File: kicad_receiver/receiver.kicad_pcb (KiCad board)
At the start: 2 copper layers, 60 x 50 mm, 64 parts, among them J1 Conn_01x05_Male, J2 M1+, J3 M1-, J4 M2+, J5 M2-, J6 CHG+5V, J7 CHG-, J8 BAT+, J9 BAT-, Q1 BSS138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

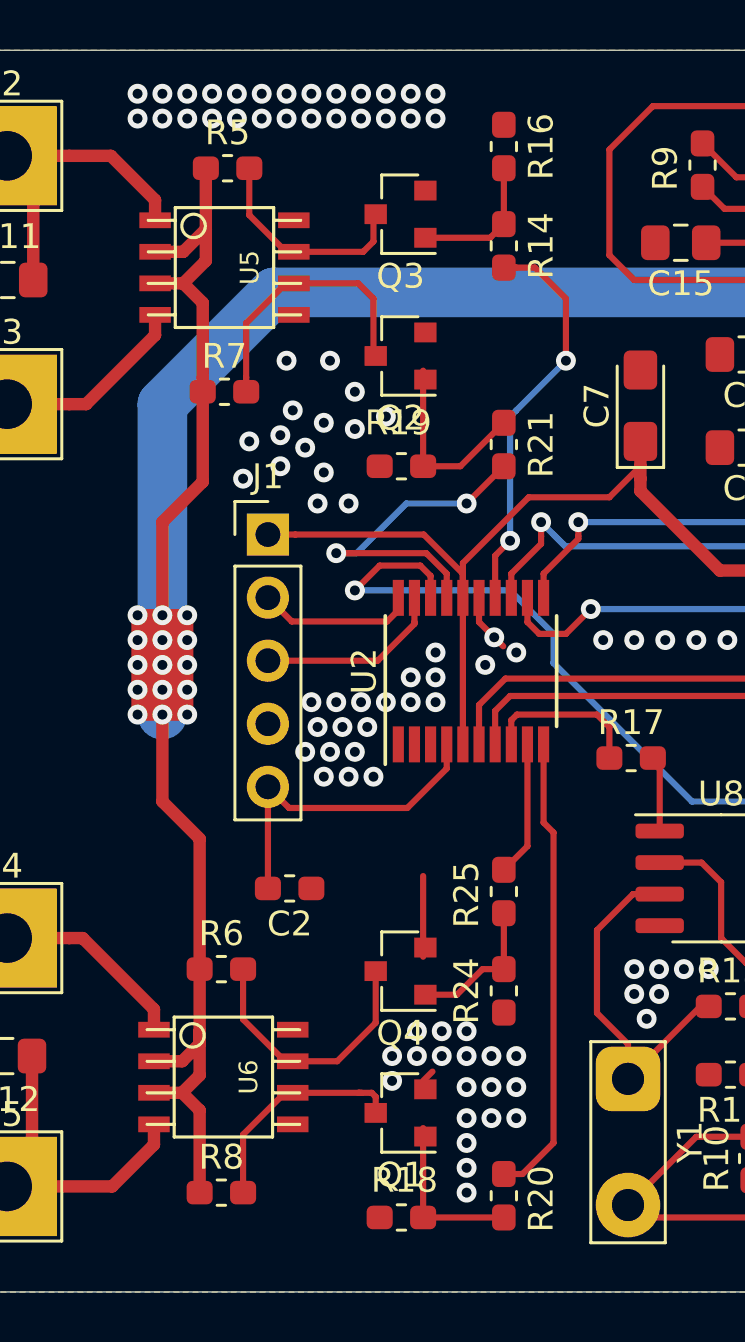
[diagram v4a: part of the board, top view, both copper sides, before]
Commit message: mosfets removed, now use pure pwm signals
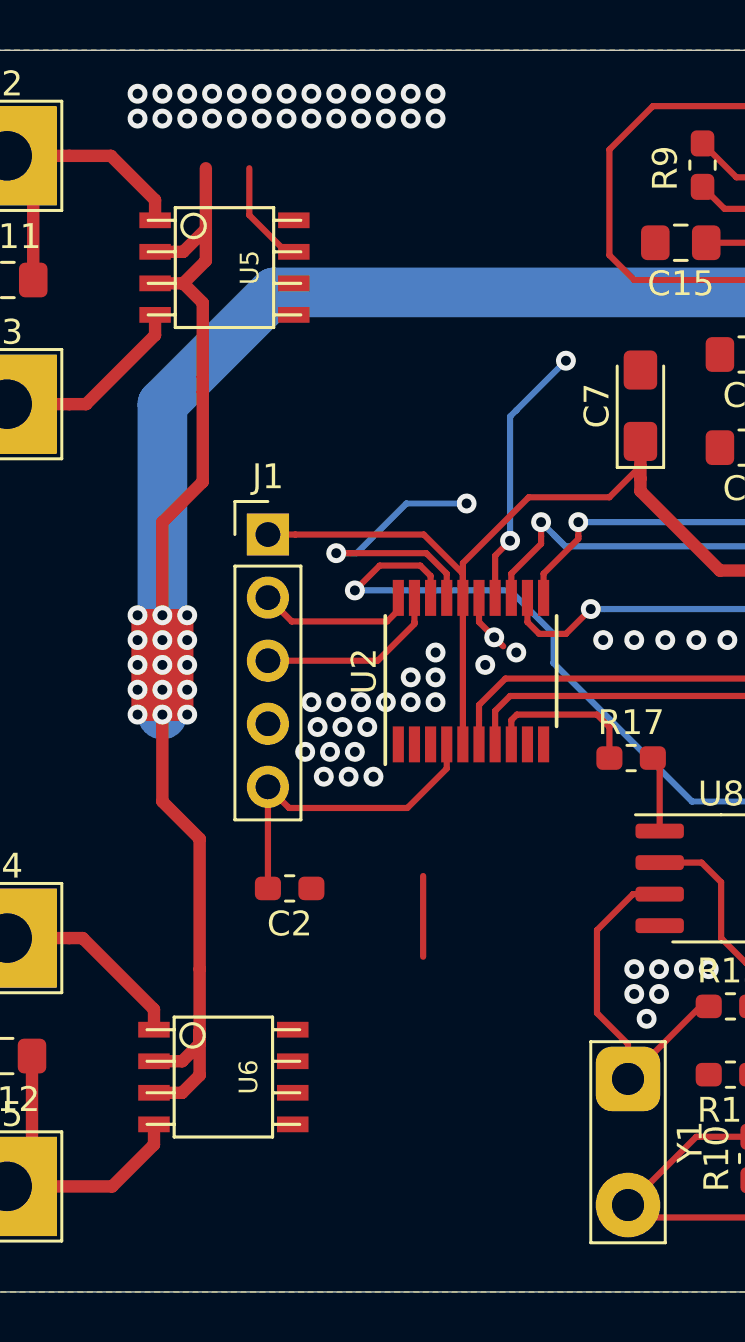
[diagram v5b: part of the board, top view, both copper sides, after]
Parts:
- removed Q1, Q2, Q3, Q4: BSS138, Package_TO_SOT_SMD:SOT-23
- removed R14, R20, R21, R25: 1k, Resistor_SMD:R_0603_1608Metric_Pad1.05x0.95mm_HandSolder
- removed R16, R18, R19, R24, R5, R6, R7, R8: 10k, Resistor_SMD:R_0603_1608Metric_Pad1.05x0.95mm_HandSolder
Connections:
- U5 pad 6: Net-(Q2-Pad3) -> FB_PWM
- U5 pad 7: Net-(Q3-Pad3) -> FF_PWM
- U6 pad 6: Net-(Q1-Pad3) -> TURN_LEFT
- U6 pad 7: Net-(Q4-Pad3) -> TURN_RIGHT
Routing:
- net TURN_LEFT: track 18.7 -> 0.00 mm
- net Net-(Q4-Pad3): track 10.8 -> 0.00 mm
- net Net-(Q2-Pad3): track 10.8 -> 0.00 mm
- net Net-(Q1-Pad3): track 9.21 -> 0.00 mm
- net Net-(Q3-Pad3): track 8.81 -> 0.00 mm
- net Net-(Q2-Pad1): track 7.82 -> 0.00 mm
- net Net-(Q1-Pad1): track 7.20 -> 0.00 mm
- net Net-(Q4-Pad1): track 5.84 -> 0.00 mm
- net Net-(Q3-Pad1): track 5.64 -> 0.00 mm
- net TURN_RIGHT: track 5.44 -> 0.00 mm
- net BAT+: track 272.3 -> 268.0 mm
- net FB_PWM: track 14.0 -> 11.8 mm
- net FF_PWM: track 16.7 -> 15.0 mm
- net GND: track 45.9 -> 45.4 mm, vias 168 -> 134

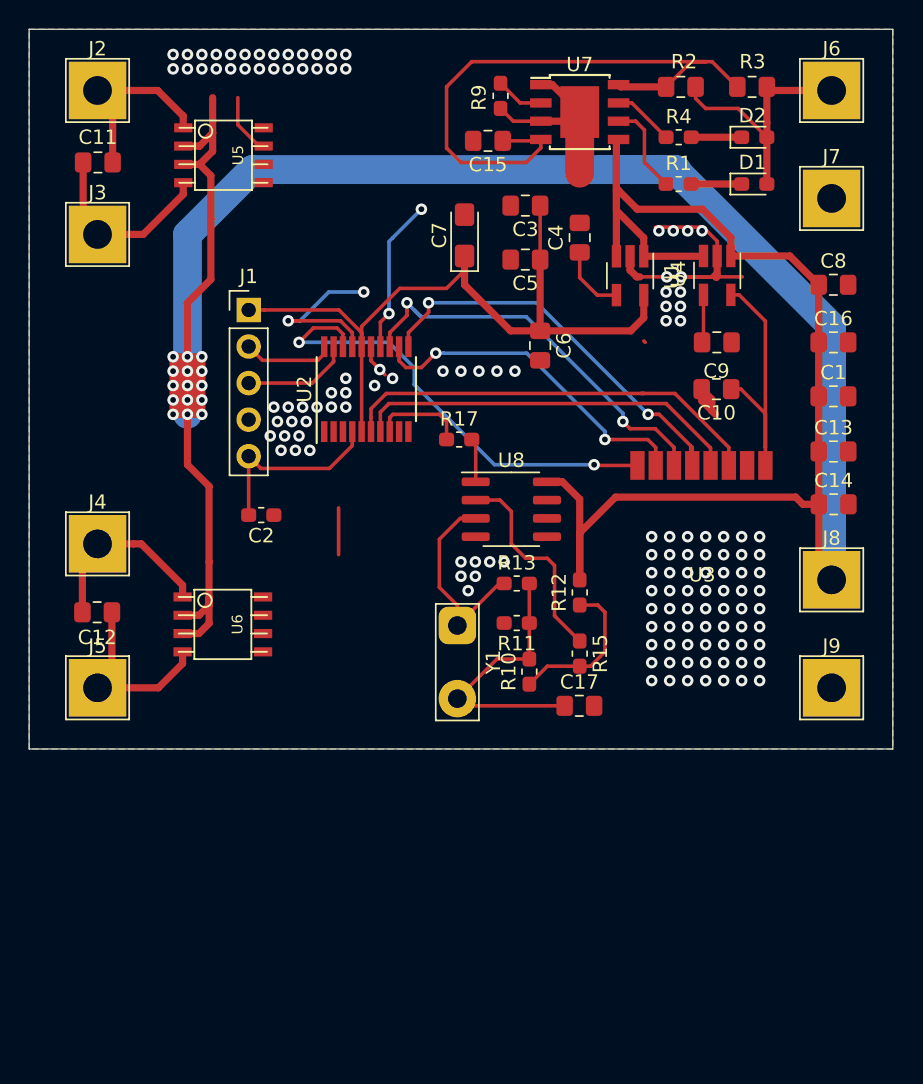
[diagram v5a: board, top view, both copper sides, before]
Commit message: lights added, new route complete
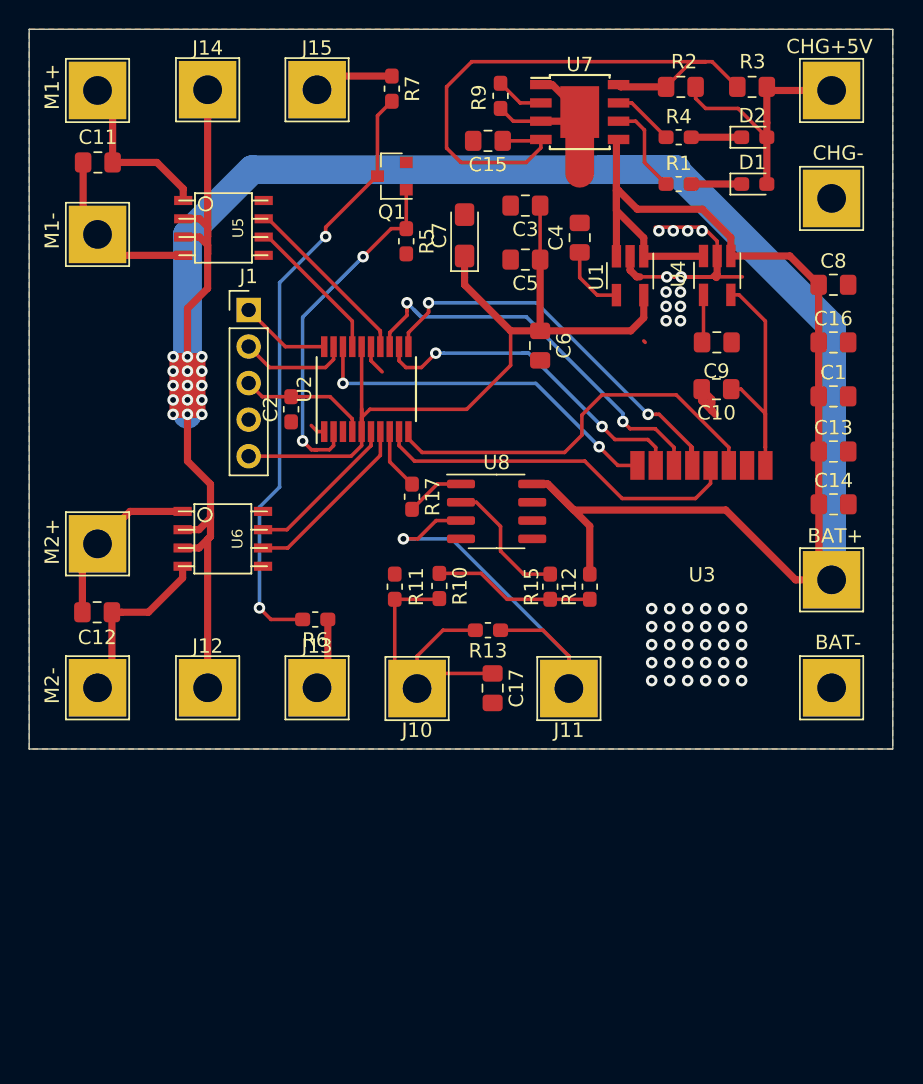
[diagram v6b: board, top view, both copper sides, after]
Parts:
- removed Y1: Crystal, TestPoint:TestPoint_2Pads_Pitch5.08mm_Drill1.3mm
- added J10: PIEZO_OUT, TestPoint:TestPoint_THTPad_4.0x4.0mm_Drill2.0mm, F.Cu at (153.9, 120.8)
- added J11: PIEZO_IN, TestPoint:TestPoint_THTPad_4.0x4.0mm_Drill2.0mm, F.Cu at (164.5, 120.8)
- added J12: LED1+, TestPoint:TestPoint_THTPad_4.0x4.0mm_Drill2.0mm, F.Cu at (139.4, 120.8)
- added J13: LED1-, TestPoint:TestPoint_THTPad_4.0x4.0mm_Drill2.0mm, F.Cu at (147.0, 120.8)
- added J14: LED2+, TestPoint:TestPoint_THTPad_4.0x4.0mm_Drill2.0mm, F.Cu at (139.4, 79.2)
- added J15: LED2-, TestPoint:TestPoint_THTPad_4.0x4.0mm_Drill2.0mm, F.Cu at (147.0, 79.2)
- added Q1: BSS138, Package_TO_SOT_SMD:SOT-23, F.Cu at (152.2, 85.2)
- added R5: 10k, Resistor_SMD:R_0603_1608Metric_Pad1.05x0.95mm_HandSolder, F.Cu at (153.2, 89.7)
- added R6: 100, Resistor_SMD:R_0603_1608Metric_Pad1.05x0.95mm_HandSolder, F.Cu at (146.9, 116.0)
- added R7: 100, Resistor_SMD:R_0603_1608Metric_Pad1.05x0.95mm_HandSolder, F.Cu at (152.2, 79.1)
- moved R11 8.84 mm to (152.4, 113.7), turned to 90 degrees
- moved R10 8.63 mm to (155.5, 113.7), turned to 270 degrees
- moved C2 7.64 mm to (145.2, 101.4), turned to 90 degrees
- moved C17 6.15 mm to (159.2, 120.8), turned to 270 degrees
- moved U6 5.94 mm to (140.5, 110.4)
- moved R17 5.15 mm to (153.6, 107.5), turned to 270 degrees
- moved R15 5.08 mm to (163.2, 113.7)
- moved U5 5.05 mm to (140.5, 88.8)
- moved R13 3.82 mm to (158.9, 116.8), turned to 180 degrees
- moved U8 1.04 mm to (159.5, 108.5)
- moved R12 0.81 mm to (165.9, 113.7)
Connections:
- J1 pad 1: 3v3mcu -> SWCLK
- J1 pad 2: SWCLK -> SWIO
- J1 pad 3: SWIO -> RST
- J1 pad 5: RST -> 3v3mcu
- U2 pad 10: TURN_LEFT -> NRF_CE
- U2 pad 2: (no net) -> LIGHTS
- U2 pad 6: NRF_CE -> TURN_RIGHT
- U2 pad 7: NRF_CSN -> TURN_LEFT
- U2 pad 9: TURN_RIGHT -> NRF_CSN
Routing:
- net Net-(Q1-Pad3): track 0.00 -> 42.4 mm, vias 0 -> 2
- net LIGHTS: track 0.00 -> 24.5 mm, vias 0 -> 2
- net Net-(J11-Pad1): track 14.1 -> 29.4 mm, vias 0 -> 1
- net TURN_LEFT: track 0.00 -> 12.5 mm
- net TURN_RIGHT: track 0.00 -> 10.9 mm
- net NRF_IRQ: track 32.2 -> 25.4 mm
- net 3v3mcu: track 52.0 -> 58.3 mm
- net Net-(J15-Pad1): track 0.00 -> 5.59 mm
- net Net-(R15-Pad1): track 14.6 -> 9.27 mm
- net Net-(J13-Pad1): track 0.00 -> 5.06 mm
- net RST: track 13.3 -> 9.11 mm
- net BAT+: track 268.0 -> 271.6 mm
- net Net-(C17-Pad1): track 19.3 -> 22.5 mm
- net FF_PWM: track 15.0 -> 12.4 mm, vias 2 -> 0
- net GND: track 45.4 -> 42.9 mm, vias 134 -> 42
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
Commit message: layout refactored, logos added
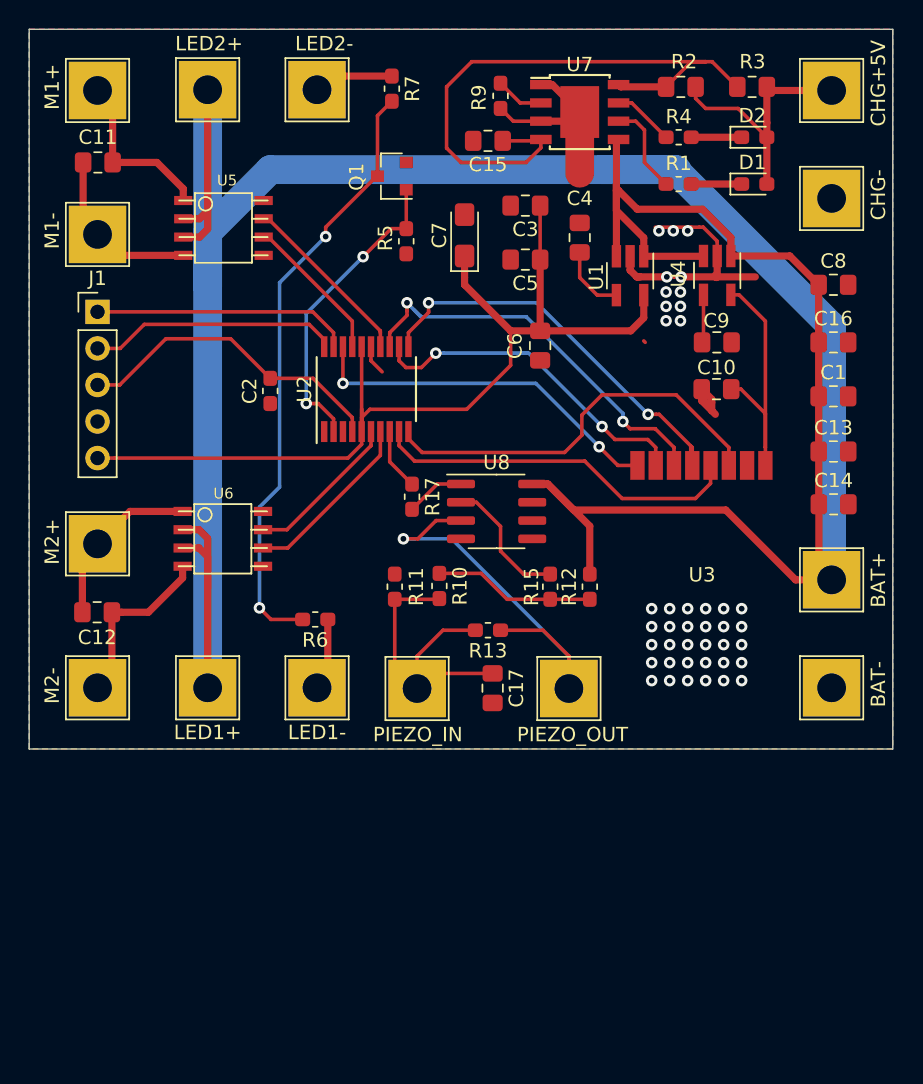
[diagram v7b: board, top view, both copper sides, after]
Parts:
- added REF**: KiCad-Logo2_8mm_SilkScreen, Symbol:KiCad-Logo2_8mm_SilkScreen, B.Cu at (169.8, 108.0)
- J10: value PIEZO_OUT -> PIEZO_IN
- J11: value PIEZO_IN -> PIEZO_OUT
- moved J1 10.5 mm to (131.8, 94.6)
- moved C2 1.93 mm to (143.8, 100.1)
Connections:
- J1 pad 1: SWCLK -> SWIO
- J1 pad 2: SWIO -> SWCLK
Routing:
- net BAT+: track 271.6 -> 236.0 mm, vias 15 -> 0
- net RST: track 9.11 -> 22.3 mm
- net SWCLK: track 6.31 -> 17.4 mm
- net 3v3mcu: track 58.3 -> 68.8 mm
- net SWIO: track 7.62 -> 18.0 mm
- net GND: track 42.9 -> 49.1 mm, vias 42 -> 41
- net LIGHTS: track 24.5 -> 21.6 mm
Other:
- board text added: "https://github.com/ vvviperrr/nrf24_remote_car"
